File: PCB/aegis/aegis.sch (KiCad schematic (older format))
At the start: 106 parts, among them Q1 TIP120, U1 ProMicro

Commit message: save
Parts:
- added LEDS1: Connector_Generic_Conn_01x03, Connector:FanPinHeader_1x03_P2.54mm_Vertical, symbol corne-classic-cache:Connector_Generic_Conn_01x03
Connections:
- net GND: now also LEDS1.3 (Pin_3)
- net LED: now also LEDS1.2 (Pin_2)
- net VCC: now also LEDS1.1 (Pin_1)
- net at LED3.2 (DOUT): now also LED4.4 (DIN)
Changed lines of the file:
@@
 SDA
-$Comp
-L SK6812MINI-E:SK6812MINI-E LED1
-U 1 1 5F95B6F7
-P 1150 3850
-F 0 "LED1" H 1494 3896 50  0000 L CNN
-F 1 "SK6812MINI-E" H 1494 3805 50  0000 L CNN
-F 2 "footprints:INV-YS-SK6812MINI-" H 1500 3650 50  0001 C CNN
-F 3 "" H 1500 3650 50  0001 C CNN
-	1    1150 3850
-	1    0    0    -1
-$EndComp
 $Comp
 L SK6812MINI-E:SK6812MINI-E LED2
@@
 	1    0    0    -1
 $EndComp
-Text GLabel 1450 3850 1    50   Input ~ 0
+Text GLabel 1150 2900 1    50   Input ~ 0
 VCC
-Text GLabel 850  3850 1    50   Input ~ 0
+Text GLabel 950  2900 1    50   Input ~ 0
 GND
-Text GLabel 1150 3550 1    50   Input ~ 0
+Text GLabel 1050 2900 1    50   Input ~ 0
 LED
 Wire Wire Line
@@
 Wire Wire Line
 	9800 3500 9950 3500
+$Comp
+L corne-classic-cache:Connector_Generic_Conn_01x03 LEDS1
+U 1 1 5FA19415
+P 1050 3100
+F 0 "LEDS1" V 922 3280 50  0000 L CNN
+F 1 "Connector_Generic_Conn_01x03" V 1013 3280 50  0000 L CNN
+F 2 "Connector:FanPinHeader_1x03_P2.54mm_Vertical" H 1050 3100 50  0001 C CNN
+F 3 "" H 1050 3100 50  0001 C CNN
+	1    1050 3100
+	0    1    1    0
+$EndComp
+$Comp
+L SK6812MINI-E:SK6812MINI-E LED1
+U 1 1 5F95B6F7
+P 1150 3850
+F 0 "LED1" H 1494 3896 50  0000 L CNN
+F 1 "SK6812MINI-E" H 1494 3805 50  0000 L CNN
+F 2 "footprints:INV-YS-SK6812MINI-" H 1500 3650 50  0001 C CNN
+F 3 "" H 1500 3650 50  0001 C CNN
+	1    1150 3850
+	1    0    0    -1
+$EndComp
+Wire Wire Line
+	950  2900 850  2900
+Wire Wire Line
+	850  2900 850  3850
+Connection ~ 850  3850
+Wire Wire Line
+	1050 2900 1050 3550
+Wire Wire Line
+	1050 3550 1150 3550
+Wire Wire Line
+	1150 2900 1450 2900
+Wire Wire Line
+	1450 2900 1450 3850
+Connection ~ 1450 3850
+Wire Wire Line
+	1150 5300 1150 5350
 $EndSCHEMATC

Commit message: update
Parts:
- Solenoide1: footprint Connector_PinHeader_1.00mm:PinHeader_1x02_P1.00mm_Vertical -> Connector_PinHeader_1.27mm:PinHeader_1x02_P1.27mm_Horizontal
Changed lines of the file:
@@
 F 0 "Solenoide1" V 9245 2950 50  0000 C CNN
 F 1 "Motor_DC" V 9154 2950 50  0000 C CNN
-F 2 "Connector_PinHeader_1.00mm:PinHeader_1x02_P1.00mm_Vertical" H 8950 2910 50  0001 C CNN
+F 2 "Connector_PinHeader_1.27mm:PinHeader_1x02_P1.27mm_Horizontal" H 8950 2910 50  0001 C CNN
 F 3 "~" H 8950 2910 50  0001 C CNN
 	1    8950 3000

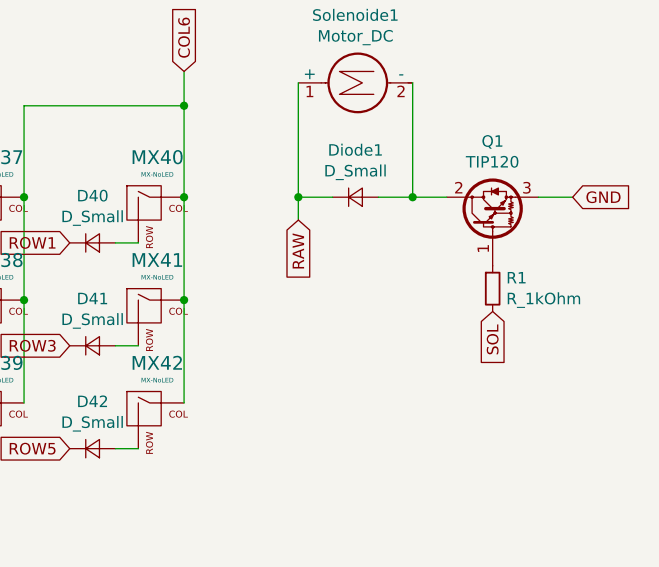
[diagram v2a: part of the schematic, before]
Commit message: update PCB to v1.1
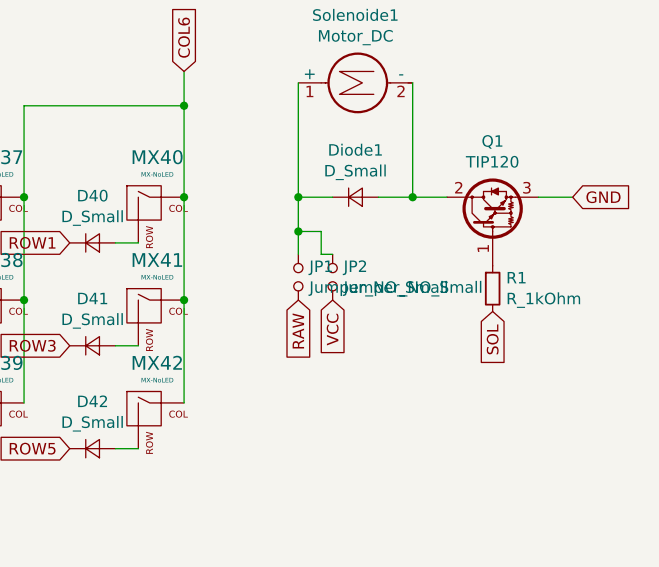
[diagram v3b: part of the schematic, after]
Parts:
- added JP1, JP2: Jumper_NO_Small, Jumper:SolderJumper-2_P1.3mm_Open_Pad1.0x1.5mm, symbol Device:Jumper_NO_Small
- Solenoide1: footprint Connector_PinHeader_1.27mm:PinHeader_1x02_P1.27mm_Horizontal -> footprints:ResetSW
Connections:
- net RAW: now also JP1.2; no longer Diode1.1 (K), Solenoide1.1 (+)
- net VCC: now also JP2.2
- new net: Diode1.1 (K), JP1.1, JP2.1, Solenoide1.1 (+)
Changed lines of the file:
@@
 Text GLabel 2550 1400 1    50   Input ~ 0
 RAW
-Text GLabel 8750 3600 3    50   Input ~ 0
+Text GLabel 8750 3950 3    50   Input ~ 0
 RAW
 $Comp
@@
 F 0 "Solenoide1" V 9245 2950 50  0000 C CNN
 F 1 "Motor_DC" V 9154 2950 50  0000 C CNN
-F 2 "Connector_PinHeader_1.27mm:PinHeader_1x02_P1.27mm_Horizontal" H 8950 2910 50  0001 C CNN
+F 2 "footprints:ResetSW" H 8950 2910 50  0001 C CNN
 F 3 "~" H 8950 2910 50  0001 C CNN
 	1    8950 3000
@@
 Wire Wire Line
 	8750 3500 8900 3500
-Wire Wire Line
-	8750 3600 8750 3500
 Connection ~ 8750 3500
 Text GLabel 9950 3500 2    50   Input ~ 0
@@
 Wire Wire Line
 	1150 5300 1150 5350
+Text GLabel 8900 3950 3    50   Input ~ 0
+VCC
+$Comp
+L Device:Jumper_NO_Small JP1
+U 1 1 5FA9D4D0
+P 8750 3850
+F 0 "JP1" V 8704 3898 50  0000 L CNN
+F 1 "Jumper_NO_Small" V 8795 3898 50  0000 L CNN
+F 2 "Jumper:SolderJumper-2_P1.3mm_Open_Pad1.0x1.5mm" H 8750 3850 50  0001 C CNN
+F 3 "~" H 8750 3850 50  0001 C CNN
+	1    8750 3850
+	0    1    1    0
+$EndComp
+$Comp
+L Device:Jumper_NO_Small JP2
+U 1 1 5FA9E67F
+P 8900 3850
+F 0 "JP2" V 8854 3898 50  0000 L CNN
+F 1 "Jumper_NO_Small" V 8945 3898 50  0000 L CNN
+F 2 "Jumper:SolderJumper-2_P1.3mm_Open_Pad1.0x1.5mm" H 8900 3850 50  0001 C CNN
+F 3 "~" H 8900 3850 50  0001 C CNN
+	1    8900 3850
+	0    1    1    0
+$EndComp
+Wire Wire Line
+	8750 3500 8750 3650
+Wire Wire Line
+	8900 3750 8850 3750
+Wire Wire Line
+	8850 3750 8850 3650
+Wire Wire Line
+	8850 3650 8750 3650
+Connection ~ 8750 3650
+Wire Wire Line
+	8750 3650 8750 3750
 $EndSCHEMATC
